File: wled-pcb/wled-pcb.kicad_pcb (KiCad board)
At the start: 2 copper layers, 28 parts, among them J2 Conn_02x03_Counter_Clockwise, J3 Screw_Terminal_01x03, J4 Screw_Terminal_01x03, J5 Screw_Terminal_01x03, J6 Screw_Terminal_01x02, J7 Screw_Terminal_01x03, K1 Relay_SPDT, Q1 BC337, U1 ESP32-DevKitC, U2 74125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

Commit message: fix some mistakes, route some traces
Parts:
- moved Q1 58.0 mm to (105.4, 95.2), turned to -90 degrees
- moved D4 48.1 mm to (166.4, 95.9)
- moved R8 40.7 mm to (162.6, 95.9), turned to 180 degrees
- moved D3 40.0 mm to (146.1, 95.9)
- moved D2 31.4 mm to (125.7, 95.9)
- moved R6 30.5 mm to (142.2, 95.9), turned to 180 degrees
- moved U2 29.0 mm to (152.4, 110.5)
- moved R5 21.7 mm to (121.9, 95.9), turned to 180 degrees
- moved R4 19.4 mm to (179.1, 130.8)
- moved J2 19.3 mm to (174.0, 110.5)
- moved F4 19.1 mm to (173.2, 118.2)
- moved U3 18.9 mm to (144.8, 110.5)
- moved J3 17.8 mm to (152.4, 137.2)
- moved J4 17.8 mm to (170.2, 137.2)
- moved F3 17.2 mm to (155.6, 118.3)
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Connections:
- R6 pad 1: Net-(D3-A) -> Net-(R6-Pad1)
- R6 pad 2: Net-(R6-Pad2) -> Net-(D3-A)
- U1 pad 16: /led4 lo -> unconnected-(U1-SD_DATA2/GPIO9-Pad16)
- U1 pad 20: /led1 lo -> unconnected-(U1-SD_CLK/GPIO6-Pad20)
- U1 pad 21: /led2 lo -> unconnected-(U1-SD_DATA0/GPIO7-Pad21)
- U1 pad 22: /led2 lo -> unconnected-(U1-SD_DATA1/GPIO8-Pad22)
- U1 pad 27: unconnected-(U1-GPIO16-Pad27) -> /led1 lo
- U1 pad 28: unconnected-(U1-GPIO17-Pad28) -> /led2 lo
- U1 pad 30: unconnected-(U1-GPIO18-Pad30) -> /led3 lo
- U1 pad 31: unconnected-(U1-GPIO19-Pad31) -> /led4 lo
- U3 pad 2: Net-(R6-Pad2) -> Net-(R6-Pad1)
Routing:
- net /5v sw: track 0.00 -> 104.3 mm
- net +5V: track 0.00 -> 72.1 mm
- net Net-(U2A-O): track 0.00 -> 36.7 mm
- net Net-(D1-A): track 0.00 -> 36.4 mm
- net Net-(U2D-O): track 0.00 -> 35.4 mm
- net Net-(U2B-O): track 0.00 -> 25.8 mm
- net Net-(U2C-O): track 0.00 -> 22.5 mm
- net Net-(D3-A): track 0.00 -> 18.6 mm
- net Net-(D2-K): track 0.00 -> 16.1 mm
- net Net-(D4-K): track 0.00 -> 16.1 mm
- net Net-(J5-Pin_1): track 0.00 -> 12.6 mm
- net Net-(J4-Pin_1): track 0.00 -> 12.6 mm
- net Net-(J3-Pin_1): track 0.00 -> 12.4 mm
- net Net-(J7-Pin_1): track 0.00 -> 12.3 mm
- net /led4 hi: track 0.00 -> 7.93 mm
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- added copper zone on B.Cu, net GND
- added copper zone on F.Cu, net GND
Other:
- board outline added: 115.6 x 52.7 mm
- board text added: "GPIO16"
- board text added: "GPIO17"
- board text added: "GPIO18"
- board text added: "GPIO19"
- board text added: "GPIO27"
- board text added: "Input"
- board text added: "Output"
- board text added: "Relay"

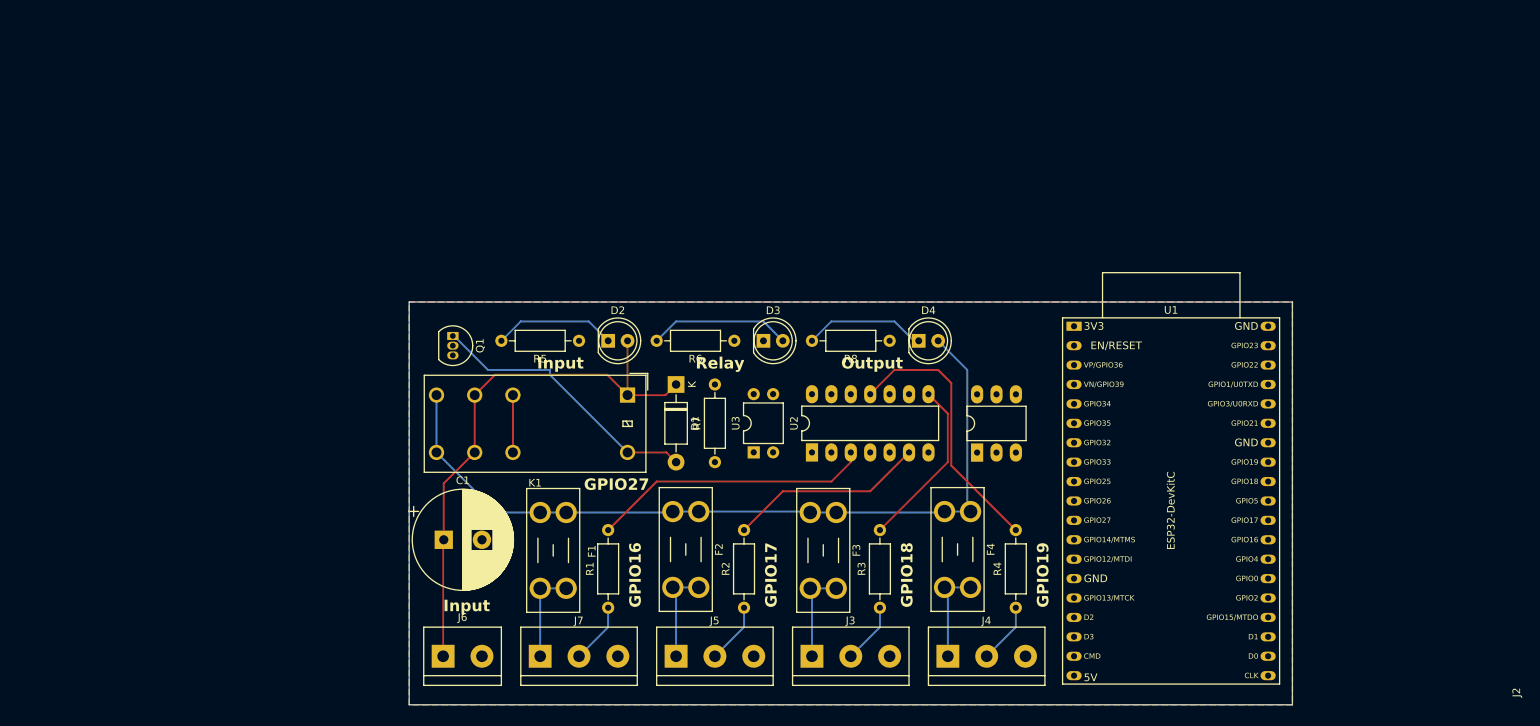
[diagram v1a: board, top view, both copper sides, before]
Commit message: Add buttons, route tracks
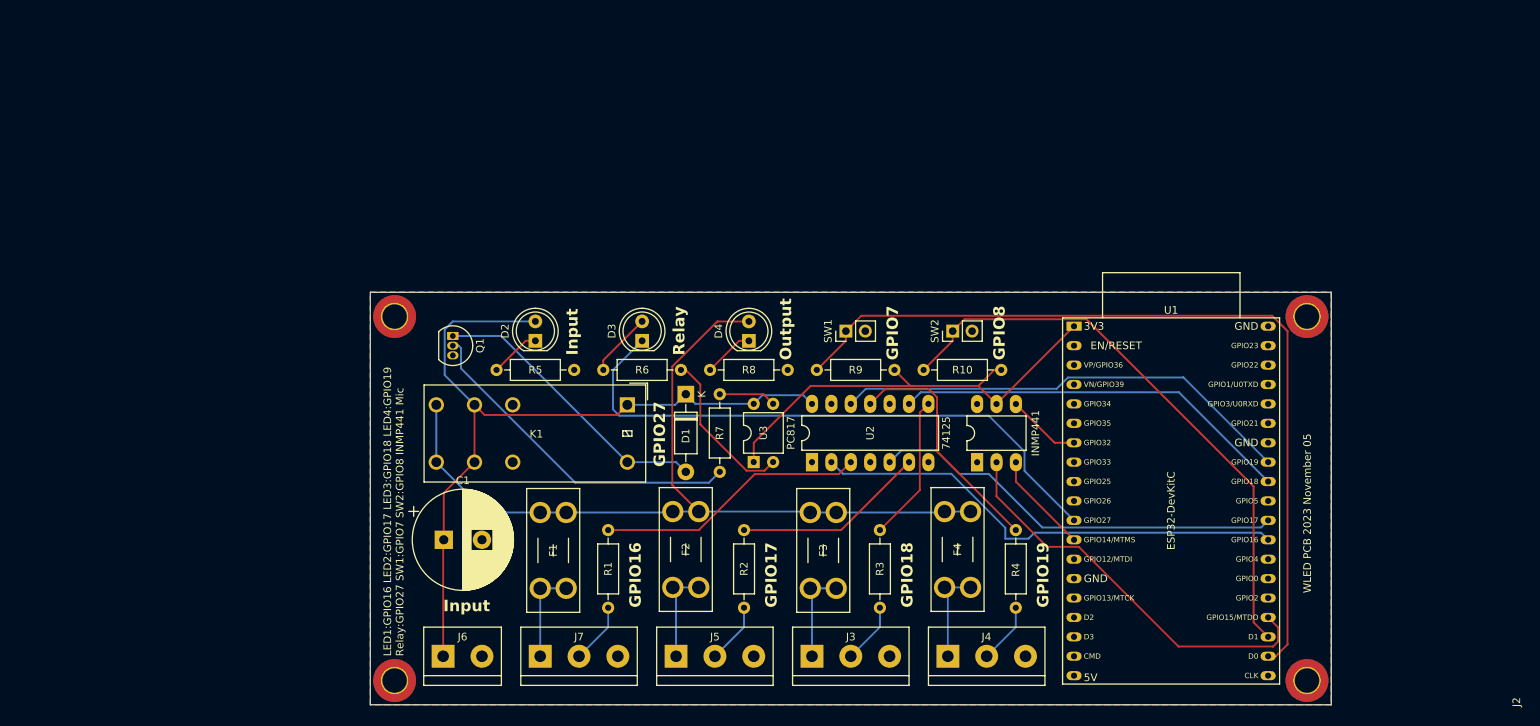
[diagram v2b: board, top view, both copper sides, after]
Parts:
- added H1: MountingHole, MountingHole:MountingHole_3.2mm_M3_DIN965_Pad_TopBottom, F.Cu at (97.8, 92.7)
- added H2: MountingHole, MountingHole:MountingHole_3.2mm_M3_DIN965_Pad_TopBottom, F.Cu at (217.2, 92.7)
- added H3: MountingHole, MountingHole:MountingHole_3.2mm_M3_DIN965_Pad_TopBottom, F.Cu at (97.8, 140.3)
- added H4: MountingHole, MountingHole:MountingHole_3.2mm_M3_DIN965_Pad_TopBottom, F.Cu at (217.2, 140.3)
- added R10: 10k, Resistor_THT:R_Axial_DIN0207_L6.3mm_D2.5mm_P10.16mm_Horizontal, F.Cu at (167.0, 99.7)
- added R9: 10k, Resistor_THT:R_Axial_DIN0207_L6.3mm_D2.5mm_P10.16mm_Horizontal, F.Cu at (153.0, 99.7)
- added SW1: SW_Push, Connector_PinHeader_2.54mm:PinHeader_1x02_P2.54mm_Vertical, F.Cu at (156.8, 94.6)
- added SW2: SW_Push, Connector_PinHeader_2.54mm:PinHeader_1x02_P2.54mm_Vertical, F.Cu at (170.8, 94.6)
- moved D4 22.2 mm to (144.1, 95.9), turned to 90 degrees
- moved D3 15.9 mm to (130.2, 95.9), turned to 90 degrees
- moved R8 13.9 mm to (149.2, 99.7)
- moved D2 9.53 mm to (116.2, 95.9), turned to 90 degrees
- moved R6 7.96 mm to (135.3, 99.7)
- moved R5 3.86 mm to (121.3, 99.7)
- moved D1 1.80 mm to (135.9, 102.9)
- moved R7 1.42 mm to (140.3, 113.0)
- moved K1 1.27 mm to (128.2, 104.3)
- moved J2 1.27 mm to (174.0, 111.8)
- moved U2 1.27 mm to (152.4, 111.8)
- moved U3 1.27 mm to (144.8, 111.8)
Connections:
- U1 pad 21: unconnected-(U1-SD_DATA0/GPIO7-Pad21) -> /sw 1
- U1 pad 22: unconnected-(U1-SD_DATA1/GPIO8-Pad22) -> /sw 2
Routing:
- net /sw 1: track 0.00 -> 110.3 mm
- net /relay trigger lo: track 0.00 -> 78.4 mm
- net /sw 2: track 0.00 -> 76.2 mm
- net /led1 lo: track 0.00 -> 62.8 mm
- net /led4 lo: track 0.00 -> 60.6 mm
- net +3.3V: track 0.00 -> 60.0 mm
- net /led2 lo: track 0.00 -> 54.7 mm
- net /mic ws: track 0.00 -> 53.4 mm
- net /led3 lo: track 0.00 -> 52.5 mm
- net Net-(Q1-B): track 0.00 -> 44.5 mm
- net +5V: track 72.1 -> 105.7 mm
- net Net-(R6-Pad1): track 0.00 -> 21.0 mm
- net /mic sck: track 0.00 -> 13.3 mm
- net Net-(D3-A): track 18.6 -> 8.45 mm
- net /mic sd: track 0.00 -> 9.70 mm
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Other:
- board size 115.6 x 52.7 mm -> 125.7 x 54 mm
- board text added: "GPIO7"
- board text added: "GPIO8"
- board text added: "INMP441"
- board text added: "LED1:GPIO16 LED2:GPIO17 LED3:GPIO18 LED4:GPIO19 Relay:GPIO27 SW1:GPIO7 SW2:GPIO8 INMP441 Mic"
- board text added: "WLED PCB 2023 November 05"

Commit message: layout board smaller than 100x100
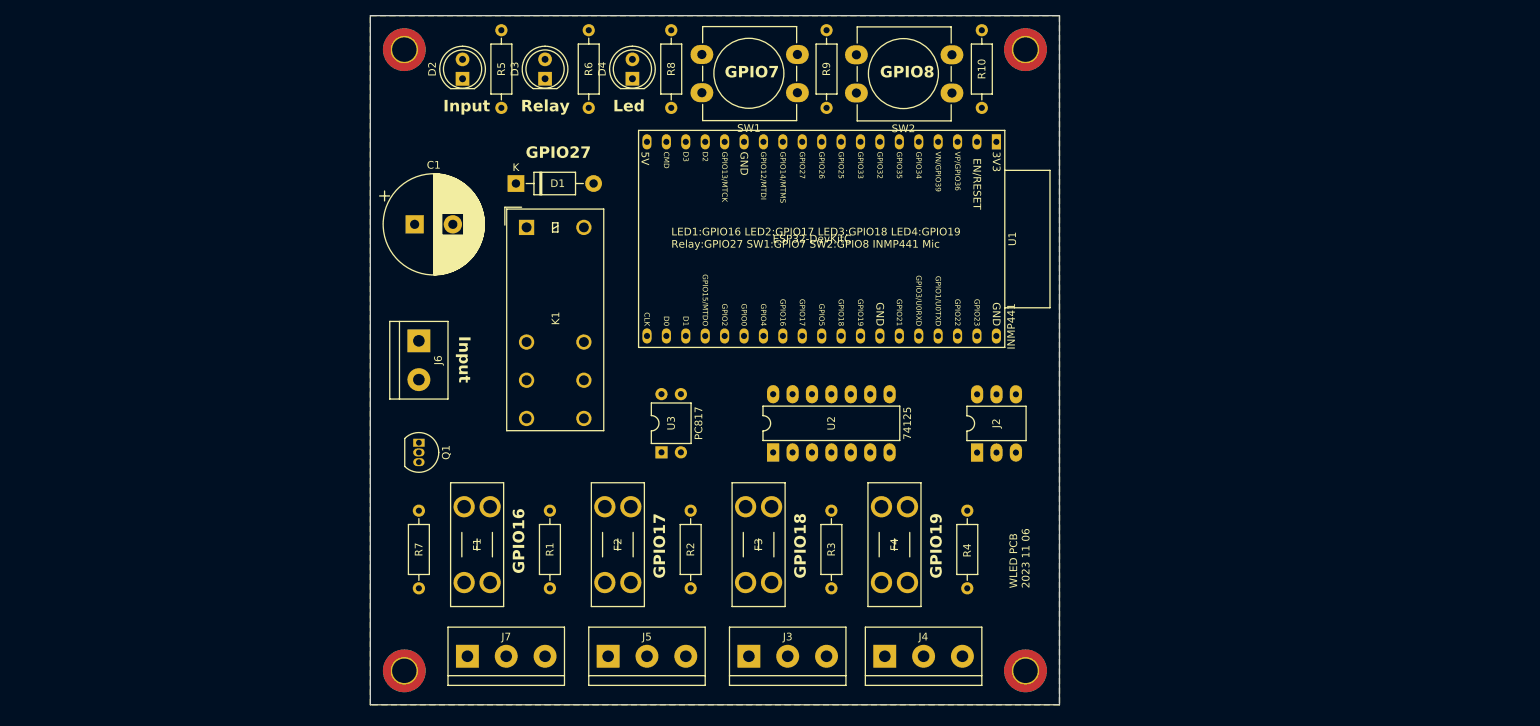
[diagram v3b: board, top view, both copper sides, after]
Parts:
- SW1, SW2: footprint Connector_PinHeader_2.54mm:PinHeader_1x02_P2.54mm_Vertical -> Button_Switch_THT:SW_PUSH-12mm_Wuerth-430476085716
- moved H2 50.8 mm to (180.3, 57.8)
- moved R7 42.2 mm to (101.0, 128.3)
- moved C1 41.5 mm to (100.4, 80.6)
- moved J6 41.4 mm to (101.0, 95.9), turned to -90 degrees
- moved D4 37.5 mm to (128.9, 61.6)
- moved R8 37.5 mm to (134.0, 65.4), turned to 90 degrees
- moved H4 36.9 mm to (180.3, 139.1)
- moved D3 36.6 mm to (117.5, 61.6)
- moved R6 36.4 mm to (123.2, 65.4), turned to 90 degrees
- moved R5 35.6 mm to (111.8, 65.4), turned to 90 degrees
- moved D2 35.6 mm to (106.7, 61.6)
- moved D1 35.4 mm to (113.7, 75.3), turned to 0 degrees
- moved R10 35.1 mm to (174.6, 65.4), turned to 90 degrees
- moved H1 34.9 mm to (99.1, 57.8)
- moved R9 34.3 mm to (154.3, 65.4), turned to 90 degrees
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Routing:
- net /5v sw: track 113.2 -> 0.00 mm
- net /sw 1: track 110.3 -> 0.00 mm
- net +5V: track 105.7 -> 0.00 mm
- net /relay trigger lo: track 78.4 -> 0.00 mm
- net /sw 2: track 76.2 -> 0.00 mm
- net /led1 lo: track 62.8 -> 0.00 mm
- net /led4 lo: track 60.6 -> 0.00 mm
- net +3.3V: track 60.0 -> 0.00 mm
- net /led2 lo: track 54.7 -> 0.00 mm
- net /mic ws: track 53.4 -> 0.00 mm
- net /led3 lo: track 52.5 -> 0.00 mm
- net Net-(Q1-B): track 44.5 -> 0.00 mm
- net Net-(D1-A): track 37.8 -> 0.00 mm
- net Net-(U2A-O): track 35.4 -> 0.00 mm
- net Net-(U2D-O): track 31.6 -> 0.00 mm
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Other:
- board size 125.7 x 54 mm -> 90.2 x 90.2 mm
- board text added: "Led"
- board text added: "WLED PCB 2023 11 06"
- board text removed: "Output"
- board text removed: "WLED PCB 2023 November 05"

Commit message: route tracks
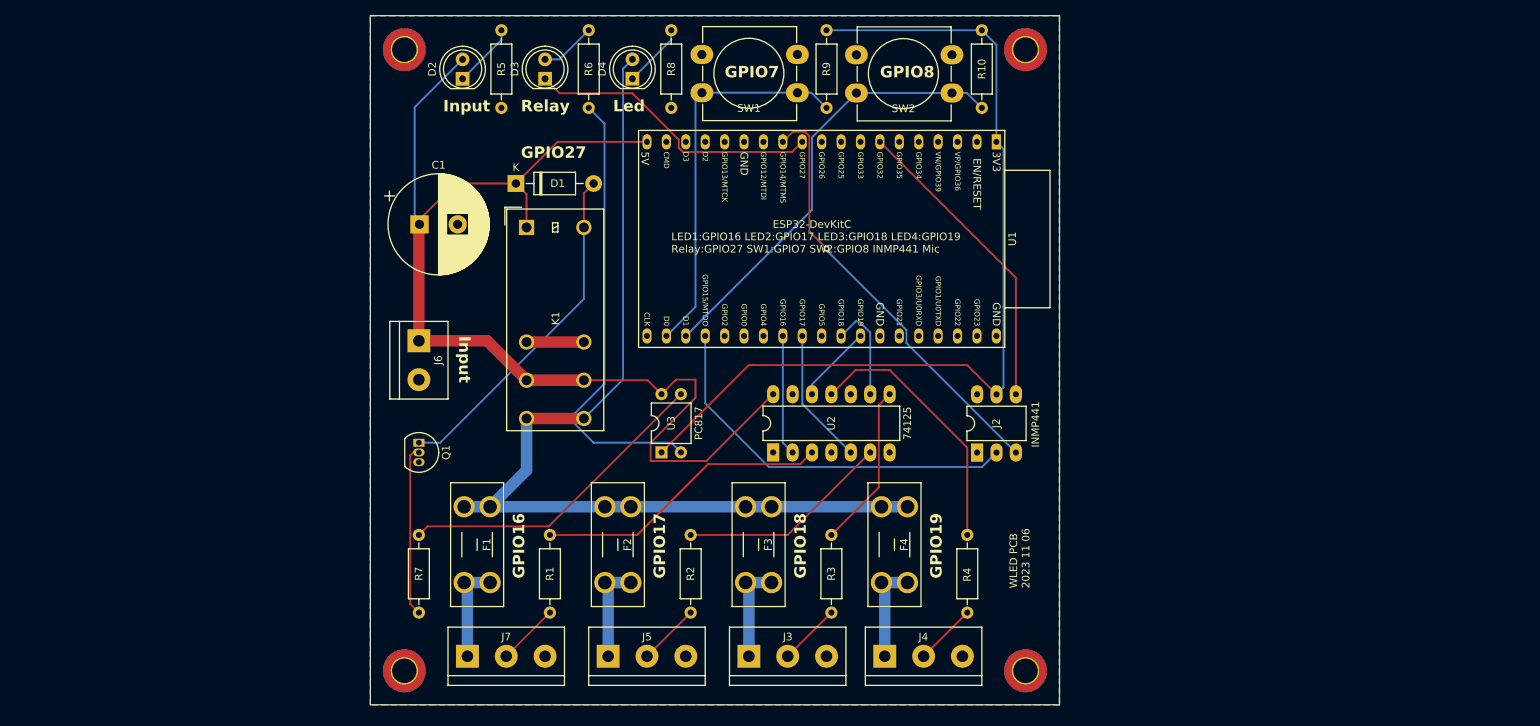
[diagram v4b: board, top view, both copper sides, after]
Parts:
- moved R1 3.17 mm to (118.1, 131.4)
- moved R2 3.17 mm to (136.5, 131.4)
- moved R3 3.17 mm to (154.9, 131.4)
- moved R4 3.17 mm to (172.7, 131.4)
- moved R7 3.17 mm to (101.0, 131.4)
- moved C1 0.64 mm to (101.0, 80.6)
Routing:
- net +5V: track 0.00 -> 153.4 mm
- net /5v sw: track 0.00 -> 128.7 mm
- net +3.3V: track 0.00 -> 119.7 mm
- net Net-(R6-Pad1): track 0.00 -> 59.4 mm
- net /sw 2: track 0.00 -> 58.3 mm
- net /mic sck: track 0.00 -> 57.0 mm, vias 0 -> 1
- net /mic ws: track 0.00 -> 51.2 mm
- net /sw 1: track 0.00 -> 50.9 mm
- net Net-(D1-A): track 0.00 -> 45.0 mm
- net Net-(R7-Pad2): track 0.00 -> 41.9 mm
- net /mic sd: track 0.00 -> 40.4 mm
- net /relay trigger lo: track 0.00 -> 38.8 mm
- net Net-(U2A-O): track 0.00 -> 38.8 mm
- net Net-(U2D-O): track 0.00 -> 34.7 mm
- net Net-(U2B-O): track 0.00 -> 28.0 mm
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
